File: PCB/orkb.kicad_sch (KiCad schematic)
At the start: 109 parts, among them J1 USB_C_Receptacle_USB2.0, P1 OLED, SW1 MXHS, SW10 MXHS, SW11 MXHS, SW12 MXHS, SW13 MXHS, SW14 MXHS, SW15 MXHS, SW16 MXHS, SW17 MXHS, SW18 MXHS, SW19 MXHS, SW2 MXHS, SW20 MXHS, SW21 MXHS, SW22 MXHS, SW23 MXHS, SW24 MSK12C02, SW25 MSK12C02, SW3 MXHS, SW4 MXHS, SW5 MXHS, SW6 MXHS, SW7 MXHS, SW8 MXHS, SW9 MXHS, U1 ProMicro, U2 SRV05-4, U3 SRV05-4

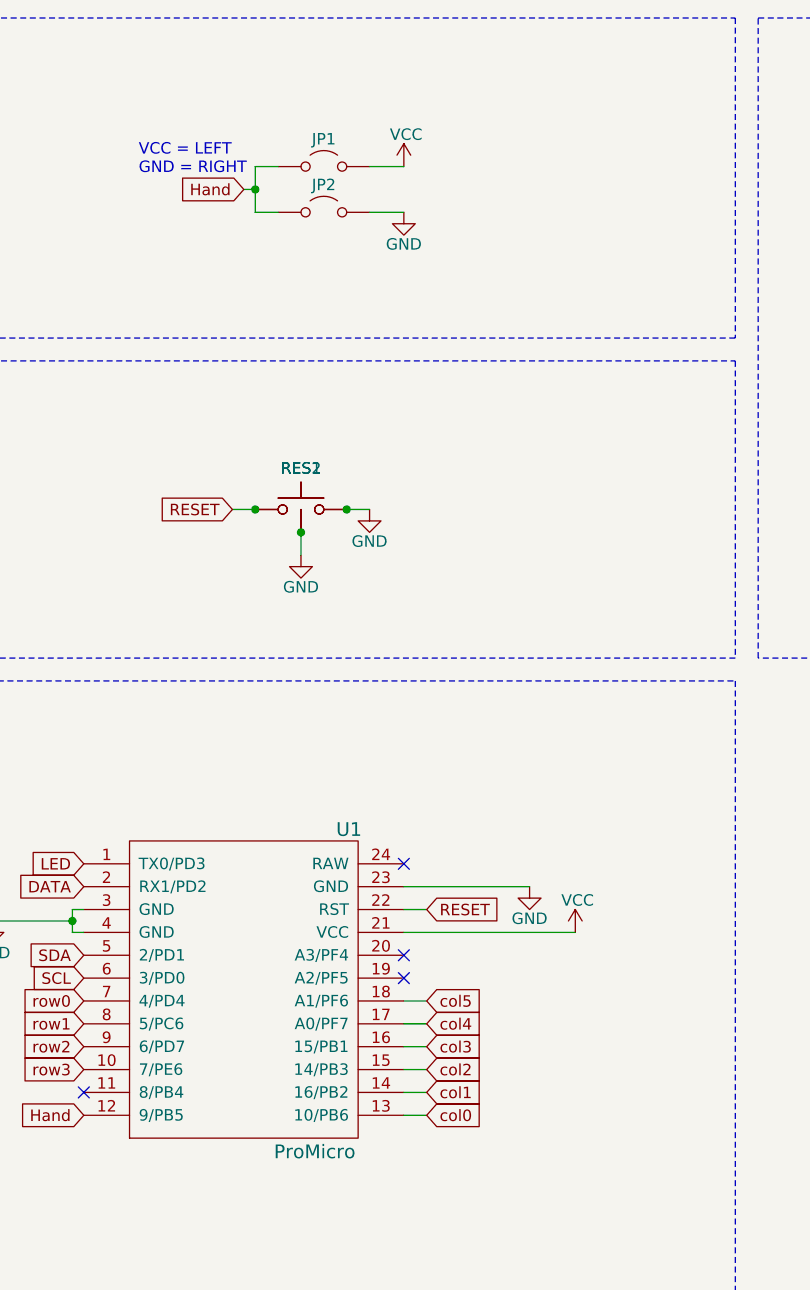
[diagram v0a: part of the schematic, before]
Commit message: Initial complete routing of PCB
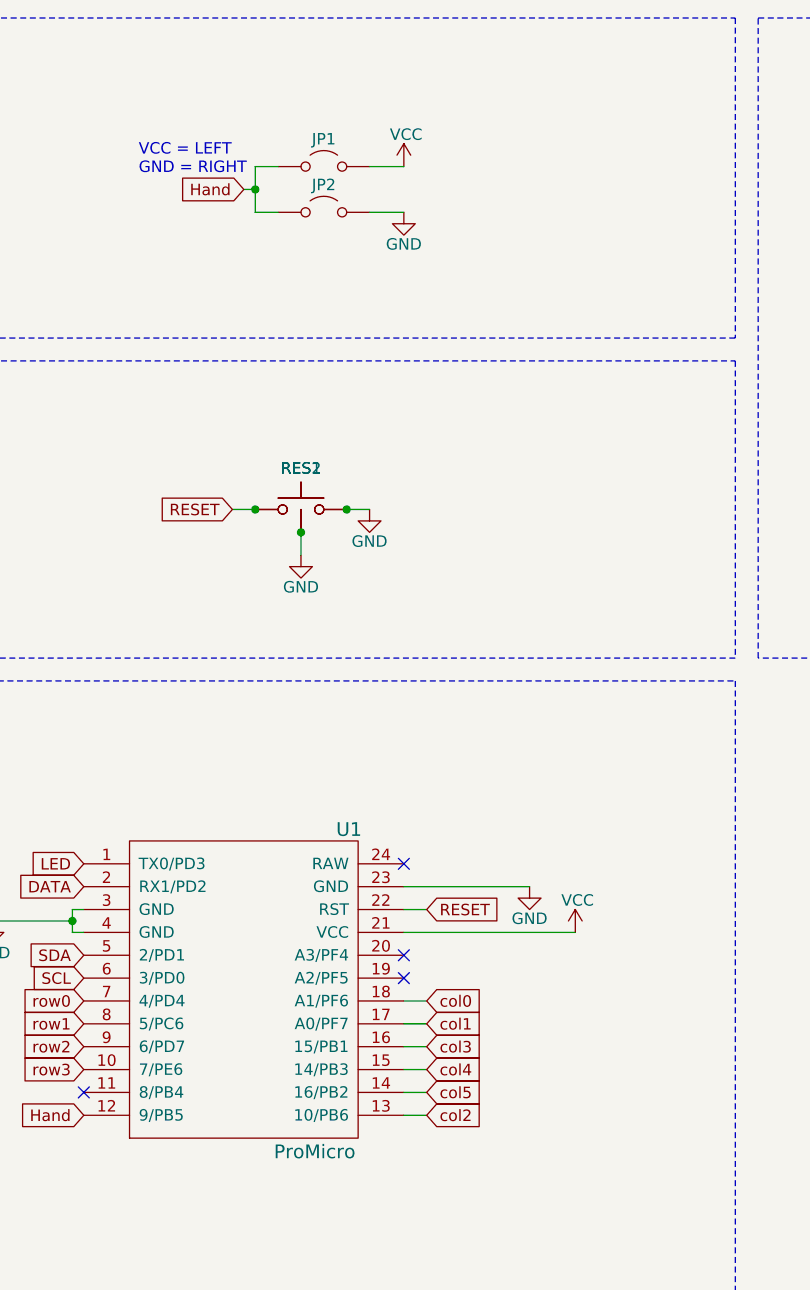
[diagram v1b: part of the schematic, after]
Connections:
- net GND: now also JP2.1 (A); no longer JP2.2 (B)
- net Hand: now also JP1.2 (B), JP2.2 (B); no longer JP1.1 (A), JP2.1 (A)
- net VCC: now also JP1.1 (A); no longer JP1.2 (B)
- net col0: now also U1.18 (A1/PF6); no longer U1.13 (10/PB6)
- net col1: now also U1.17 (A0/PF7); no longer U1.14 (16/PB2)
- net col2: now also U1.13 (10/PB6); no longer U1.15 (14/PB3)
- net col4: now also U1.15 (14/PB3); no longer U1.17 (A0/PF7)
- net col5: now also U1.14 (16/PB2); no longer U1.18 (A1/PF6)
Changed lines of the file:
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@@
 	(wire
 		(pts
+			(xy 245.11 125.73) (xy 247.65 125.73)
+		)
+		(stroke
+			(width 0)
+			(type default)
+		)
+	)
+	(wire
+		(pts
 			(xy 62.23 167.64) (xy 50.8 167.64)
 		)
@@
 	(wire
 		(pts
-			(xy 245.11 125.73) (xy 247.65 125.73)
+			(xy 101.6 105.41) (xy 101.6 113.03)
 		)
 		(stroke
@@
 	(wire
 		(pts
-			(xy 101.6 105.41) (xy 101.6 113.03)
+			(xy 245.11 130.81) (xy 247.65 130.81)
 		)
 		(stroke
@@
 	(wire
 		(pts
-			(xy 245.11 123.19) (xy 247.65 123.19)
+			(xy 90.17 240.03) (xy 90.17 241.3)
 		)
 		(stroke
@@
 	(wire
 		(pts
-			(xy 90.17 240.03) (xy 90.17 241.3)
+			(xy 44.45 214.63) (xy 46.99 214.63)
 		)
 		(stroke
@@
 	(wire
 		(pts
-			(xy 44.45 214.63) (xy 46.99 214.63)
+			(xy 90.17 259.08) (xy 90.17 260.35)
 		)
 		(stroke
@@
 	(wire
 		(pts
-			(xy 90.17 259.08) (xy 90.17 260.35)
+			(xy 245.11 135.89) (xy 247.65 135.89)
 		)
 		(stroke
@@
 	(wire
 		(pts
-			(xy 118.11 113.03) (xy 118.11 128.27)
+			(xy 245.11 133.35) (xy 247.65 133.35)
 		)
 		(stroke
@@
 	(wire
 		(pts
-			(xy 85.09 113.03) (xy 85.09 128.27)
+			(xy 118.11 113.03) (xy 118.11 128.27)
 		)
 		(stroke
@@
 	(wire
 		(pts
-			(xy 54.61 223.52) (xy 72.39 223.52)
+			(xy 85.09 113.03) (xy 85.09 128.27)
 		)
 		(stroke
@@
 	(wire
 		(pts
-			(xy 36.83 223.52) (xy 54.61 223.52)
+			(xy 54.61 223.52) (xy 72.39 223.52)
 		)
 		(stroke
@@
 	(wire
 		(pts
-			(xy 115.57 250.19) (xy 118.11 250.19)
+			(xy 36.83 223.52) (xy 54.61 223.52)
 		)
 		(stroke
@@
 	(wire
 		(pts
-			(xy 245.11 133.35) (xy 247.65 133.35)
+			(xy 115.57 250.19) (xy 118.11 250.19)
 		)
 		(stroke
@@
 	(wire
 		(pts
+			(xy 245.11 128.27) (xy 247.65 128.27)
+		)
+		(stroke
+			(width 0)
+			(type default)
+		)
+	)
+	(wire
+		(pts
 			(xy 80.01 232.41) (xy 82.55 232.41)
 		)
@@
 	(wire
 		(pts
-			(xy 245.11 135.89) (xy 247.65 135.89)
-		)
-		(stroke
-			(width 0)
-			(type default)
-		)
-	)
-	(wire
-		(pts
 			(xy 50.8 181.61) (xy 62.23 181.61)
 		)
@@
 	(wire
 		(pts
-			(xy 245.11 130.81) (xy 247.65 130.81)
-		)
-		(stroke
-			(width 0)
-			(type default)
-		)
-	)
-	(wire
-		(pts
 			(xy 111.76 45.72) (xy 114.3 45.72)
 		)
@@
 	(wire
 		(pts
-			(xy 245.11 128.27) (xy 247.65 128.27)
+			(xy 245.11 123.19) (xy 247.65 123.19)
 		)
 		(stroke
@@
 	(global_label "col0"
 		(shape input)
-		(at 247.65 135.89 0)
+		(at 247.65 123.19 0)
 		(fields_autoplaced yes)
 		(effects
@@
 		)
 		(property "Intersheetrefs" "${INTERSHEET_REFS}"
-			(at 254.7475 135.89 0)
+			(at 254.7475 123.19 0)
 			(effects
 				(font
@@
 	(global_label "col1"
 		(shape input)
-		(at 247.65 133.35 0)
+		(at 247.65 125.73 0)
 		(fields_autoplaced yes)
 		(effects
@@
 		)
 		(property "Intersheetrefs" "${INTERSHEET_REFS}"
-			(at 254.7475 133.35 0)
+			(at 254.7475 125.73 0)
 			(effects
 				(font
@@
 	(global_label "col4"
 		(shape input)
-		(at 247.65 125.73 0)
+		(at 247.65 130.81 0)
 		(fields_autoplaced yes)
 		(effects
@@
 		)
 		(property "Intersheetrefs" "${INTERSHEET_REFS}"
-			(at 254.7475 125.73 0)
+			(at 254.7475 130.81 0)
 			(effects
 				(font
@@
 	(global_label "col2"
 		(shape input)
-		(at 247.65 130.81 0)
+		(at 247.65 135.89 0)
 		(fields_autoplaced yes)
 		(effects
@@
 		)
 		(property "Intersheetrefs" "${INTERSHEET_REFS}"
-			(at 254.7475 130.81 0)
+			(at 254.7475 135.89 0)
 			(effects
 				(font
@@
 	(global_label "col5"
 		(shape input)
-		(at 247.65 123.19 0)
+		(at 247.65 133.35 0)
 		(fields_autoplaced yes)
 		(effects
@@
 		)
 		(property "Intersheetrefs" "${INTERSHEET_REFS}"
-			(at 254.7475 123.19 0)
+			(at 254.7475 133.35 0)
 			(effects
 				(font
@@
 		(lib_id "Jumper:Jumper_2_Open")
 		(at 236.22 35.56 0)
+		(mirror y)
 		(unit 1)
 		(exclude_from_sim yes)
@@
 		(lib_id "Jumper:Jumper_2_Open")
 		(at 236.22 30.48 0)
+		(mirror y)
 		(unit 1)
 		(exclude_from_sim yes)

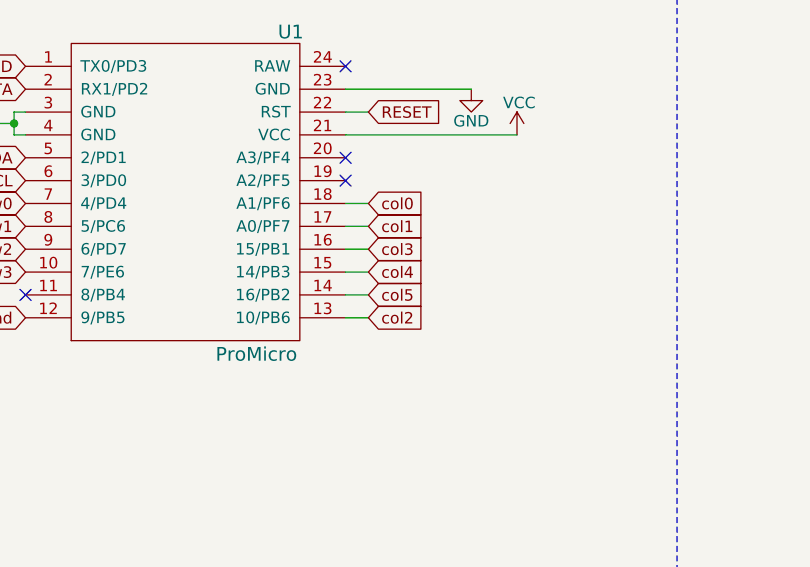
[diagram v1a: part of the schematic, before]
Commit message: Fixing column order and routing
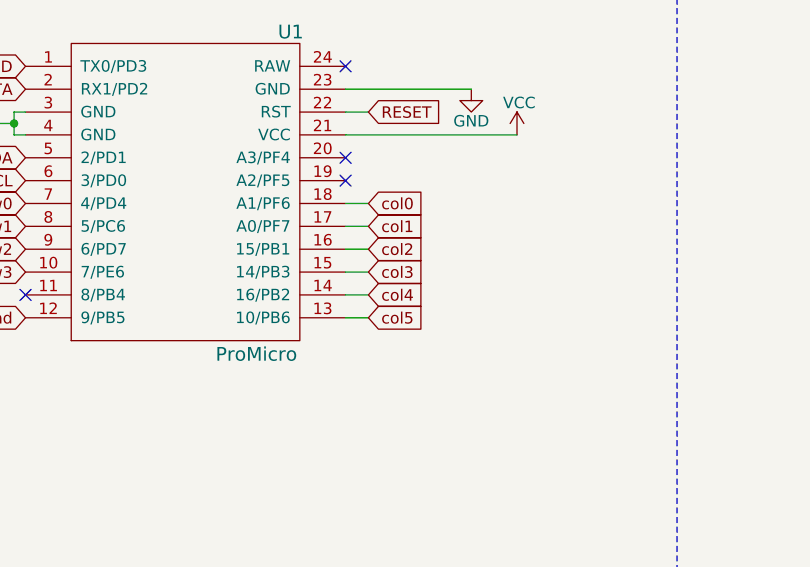
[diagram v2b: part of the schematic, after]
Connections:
- net col2: now also U1.16 (15/PB1); no longer U1.13 (10/PB6)
- net col3: now also U1.15 (14/PB3); no longer U1.16 (15/PB1)
- net col4: now also U1.14 (16/PB2); no longer U1.15 (14/PB3)
- net col5: now also U1.13 (10/PB6); no longer U1.14 (16/PB2)

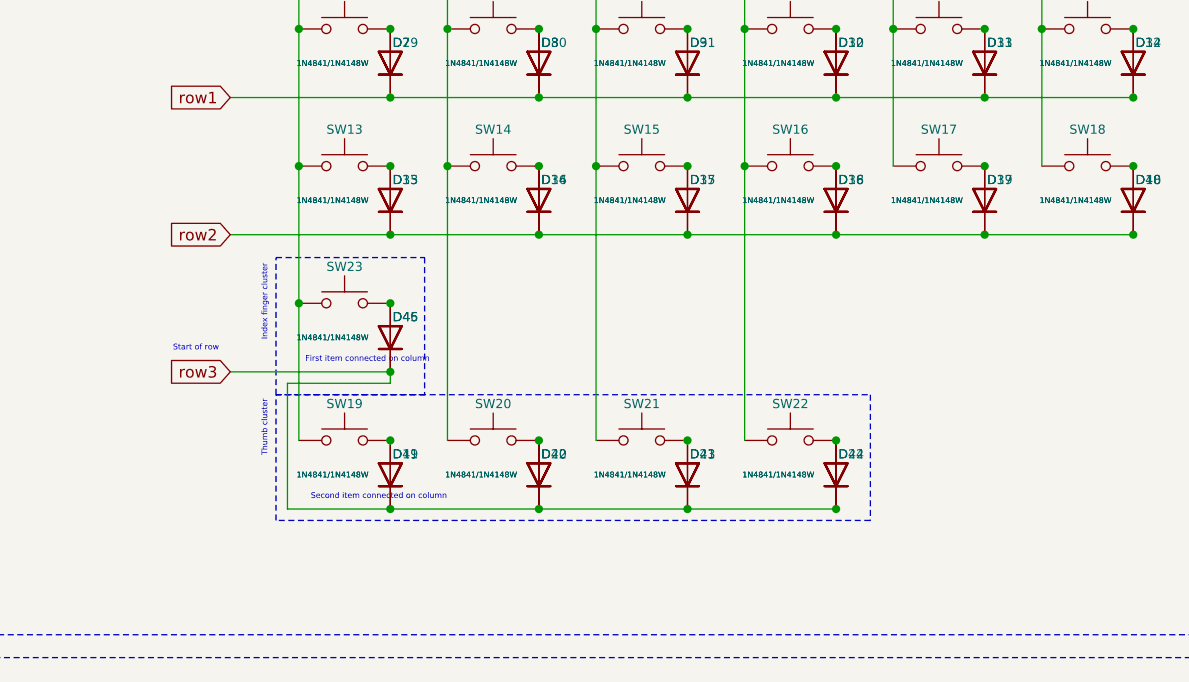
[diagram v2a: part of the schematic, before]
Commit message: Fix column routing for index/thumb cluster
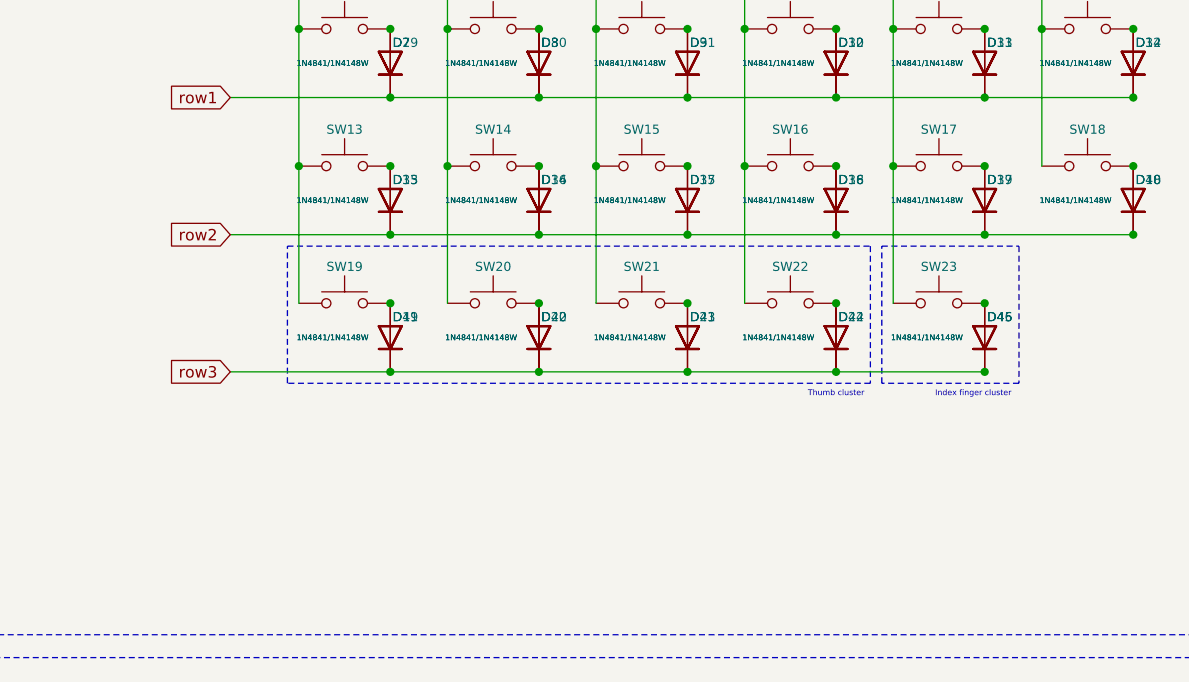
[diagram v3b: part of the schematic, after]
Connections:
- net col0: no longer SW23.1
- net col4: now also SW23.1
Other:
- note removed: "First item connected on column"
- note removed: "Second item connected on column"
- note removed: "Start of row"
- moved on the sheet: D19, D20, D21, D22, D41, D42, D43, D44, D45, D46, SW19, SW20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
